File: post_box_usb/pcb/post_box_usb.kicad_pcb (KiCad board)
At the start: 4 copper layers, 90 x 45 mm, 63 parts, among them U1 MCP1700T-3302E/MB, X1 MC146 32768Hz

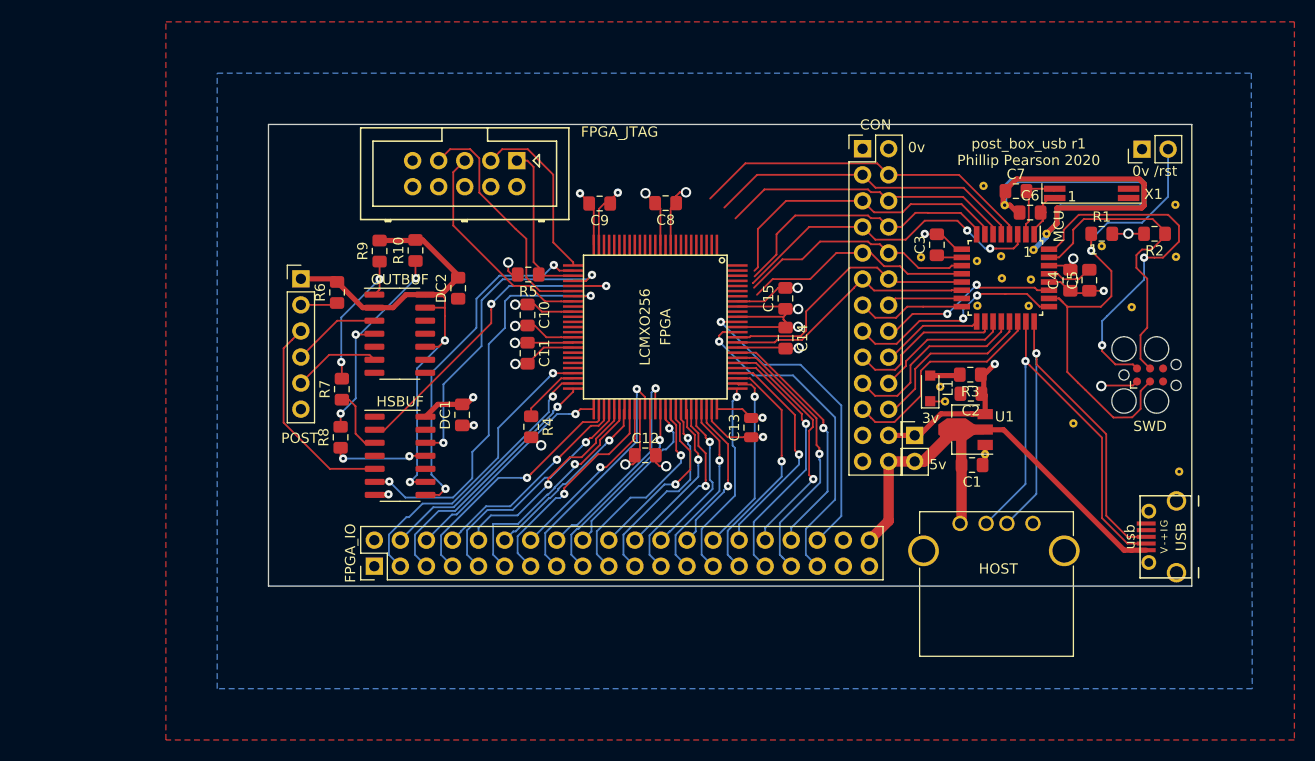
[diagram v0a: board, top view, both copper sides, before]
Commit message: Nearly done with the post_box_usb layout aside from a few TODOs in post_box_usb.py
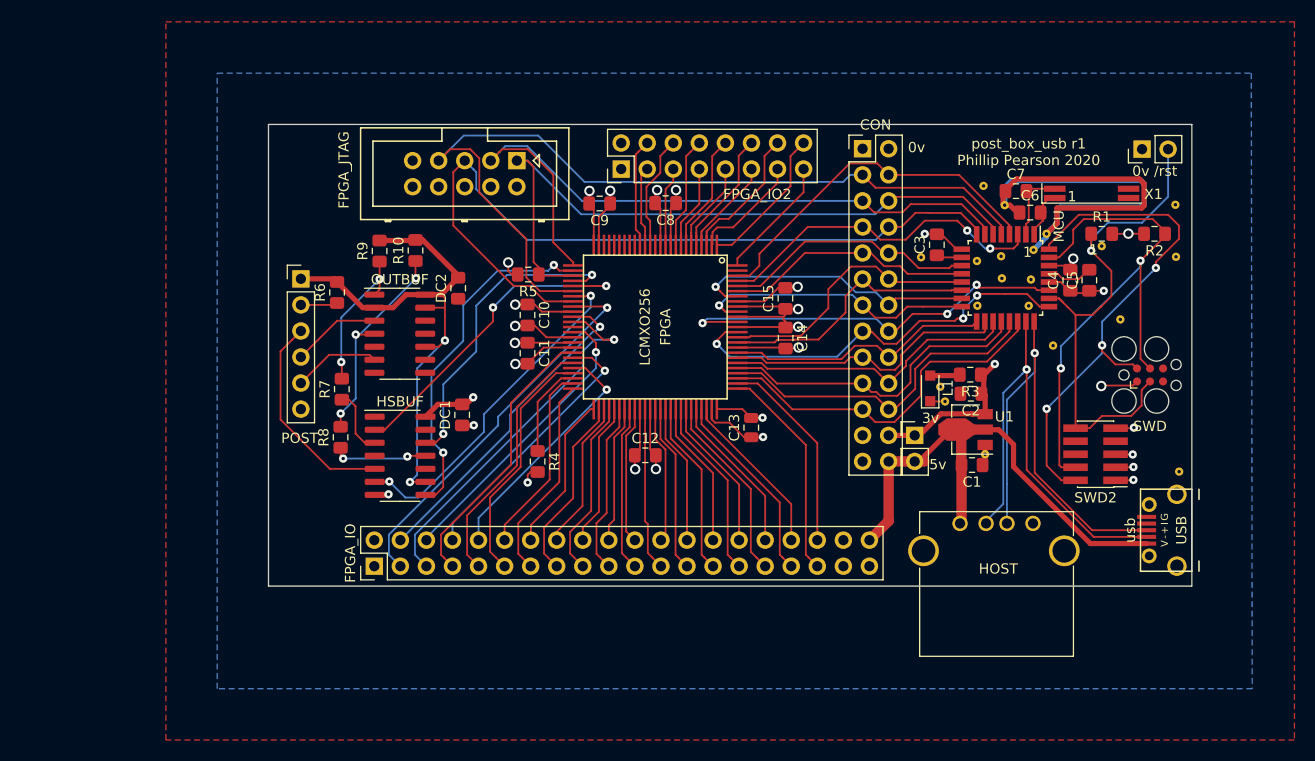
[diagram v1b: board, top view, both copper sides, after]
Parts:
- added FPGA_IO2: pins, Connector_PinHeader_2.54mm:PinHeader_2x08_P2.54mm_Vertical, F.Cu at (144.4, 134.3)
- added SWD2: swd, Connector_PinHeader_1.27mm:PinHeader_2x05_P1.27mm_Vertical_SMD, F.Cu at (190.6, 162.1)
- moved staple_single3 7.84 mm to (186.5, 151.6)
- moved R4 3.44 mm to (136.2, 162.9)
- moved staple_single11 1.63 mm to (193.0, 149.0)
- moved USB 0.65 mm to (198.0, 169.6)
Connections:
- CON pad 1: GND -> 3V3
- CON pad 3: PA04 -> fpga_TDO
- CON pad 5: PA06 -> fpga_TMS
- CON pad 6: PA05 -> fpga_TCK
- CON pad 8: PA07 -> fpga_TDI
- FPGA pad 1: (no net) -> fpga_GPIO47
- FPGA pad 100: (no net) -> fpga_GPIO46
- FPGA pad 11: (no net) -> fpga_GPIO36
- FPGA pad 14: (no net) -> fpga_GPIO37
- FPGA pad 15: (no net) -> fpga_GPIO34
- FPGA pad 16: (no net) -> fpga_GPIO35
- FPGA pad 2: (no net) -> fpga_GPIO44
- FPGA pad 3: (no net) -> fpga_GPIO45
- FPGA pad 34: (no net) -> fpga_GPIO0
- FPGA pad 36: (no net) -> fpga_GPIO1
- FPGA pad 37: (no net) -> fpga_GPIO2
- FPGA pad 38: (no net) -> fpga_OSC_in
- FPGA pad 39: (no net) -> fpga_GPIO3
- FPGA pad 4: (no net) -> fpga_GPIO42
- FPGA pad 43: (no net) -> fpga_GPIO4
- FPGA pad 44: (no net) -> fpga_GPIO5
- FPGA pad 45: (no net) -> fpga_GPIO6
- FPGA pad 46: (no net) -> fpga_GPIO7
- FPGA pad 47: fpga_GPIO0 -> fpga_GPIO8
- FPGA pad 49: fpga_GPIO1 -> fpga_GPIO9
- FPGA pad 5: (no net) -> fpga_GPIO43
- FPGA pad 50: fpga_GPIO2 -> fpga_GPIO10
- FPGA pad 51: fpga_GPIO3 -> fpga_GPIO11
- FPGA pad 52: fpga_GPIO4 -> fpga_GPIO12
- FPGA pad 53: fpga_GPIO5 -> fpga_GPIO13
- FPGA pad 54: fpga_GPIO6 -> fpga_GPIO14
- FPGA pad 55: fpga_GPIO7 -> fpga_GPIO15
- FPGA pad 56: fpga_GPIO8 -> fpga_GPIO16
- FPGA pad 57: fpga_GPIO9 -> fpga_GPIO17
- FPGA pad 58: fpga_GPIO10 -> fpga_GPIO18
- FPGA pad 59: fpga_GPIO11 -> fpga_GPIO19
- FPGA pad 6: (no net) -> fpga_GPIO40
- FPGA pad 61: fpga_GPIO12 -> fpga_GPIO20
- FPGA pad 63: fpga_GPIO13 -> fpga_GPIO21
- FPGA pad 64: fpga_GPIO14 -> fpga_GPIO22
- FPGA pad 65: fpga_GPIO15 -> fpga_GPIO23
- FPGA pad 66: fpga_GPIO16 -> fpga_GPIO24
- FPGA pad 67: fpga_GPIO17 -> fpga_GPIO25
- FPGA pad 68: fpga_GPIO18 -> fpga_GPIO26
- FPGA pad 69: fpga_GPIO19 -> fpga_GPIO27
- FPGA pad 7: (no net) -> fpga_GPIO41
- FPGA pad 70: fpga_GPIO20 -> fpga_GPIO28
- FPGA pad 71: fpga_GPIO21 -> fpga_GPIO29
- FPGA pad 72: fpga_GPIO22 -> fpga_GPIO30
- FPGA pad 73: fpga_GPIO23 -> fpga_GPIO31
- FPGA pad 76: fpga_GPIO24 -> fpga_GPIO32
- FPGA pad 77: fpga_GPIO25 -> fpga_GPIO33
- FPGA pad 78: fpga_GPIO26 -> mcu_RXD
- FPGA pad 79: fpga_GPIO27 -> mcu_TXD
- FPGA pad 8: (no net) -> fpga_GPIO38
- FPGA pad 80: fpga_GPIO28 -> PA19
- FPGA pad 81: fpga_GPIO29 -> PA18
- FPGA pad 82: fpga_GPIO30 -> want_tx
- FPGA pad 83: fpga_GPIO31 -> tx_pending
- FPGA pad 87: fpga_GPIO32 -> PA27
- FPGA pad 89: fpga_GPIO33 -> reset_in
- FPGA pad 9: (no net) -> fpga_GPIO39
- FPGA pad 91: (no net) -> fpga_MISO
- FPGA pad 94: (no net) -> fpga_SS
- FPGA pad 95: (no net) -> fpga_SCK
- FPGA pad 96: (no net) -> fpga_MOSI
- FPGA pad 97: (no net) -> last_transaction_was_input
- FPGA pad 98: (no net) -> PA03
- MCU pad 5: PA04 -> fpga_TDO
- MCU pad 6: PA05 -> fpga_TCK
- MCU pad 7: PA06 -> fpga_TMS
- MCU pad 8: PA07 -> fpga_TDI
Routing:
- net fpga_TDO: track 23.5 -> 84.4 mm
- net fpga_TDI: track 21.5 -> 77.9 mm
- net fpga_TMS: track 17.2 -> 70.6 mm
- net fpga_TCK: track 16.0 -> 67.2 mm
- net PA04: track 31.2 -> 0.00 mm
- net PA06: track 29.9 -> 0.00 mm
- net PA05: track 28.9 -> 0.00 mm
- net PA07: track 27.5 -> 0.00 mm
- net mcu_SWCLK: track 31.3 -> 54.8 mm, vias 0 -> 2
- net reset_in: track 17.7 -> 40.0 mm, vias 2 -> 3
- net fpga_SS: track 7.81 -> 28.7 mm, vias 0 -> 1
- net PA27: track 21.7 -> 40.1 mm, vias 2 -> 3
- net fpga_MISO: track 10.6 -> 27.5 mm, vias 0 -> 1
- net mcu_TXD: track 17.0 -> 33.2 mm
- net tx_pending: track 10.4 -> 26.4 mm
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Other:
- board text added: "post_box_usb r1 Copyright 2017-2020 Google Inc Designed by Phillip Pearson github.com/google/myelin-acorn-electron-hardware myelin.nz/acorn/postbox"
- board text removed: "post_box_usb Copyright 2017-2020 Google Inc Designed by Phillip Pearson github.com/google/ myelin-acorn-electron-hardware"

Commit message: post_box_usb PCB r1 finished and sent to JLCPCB
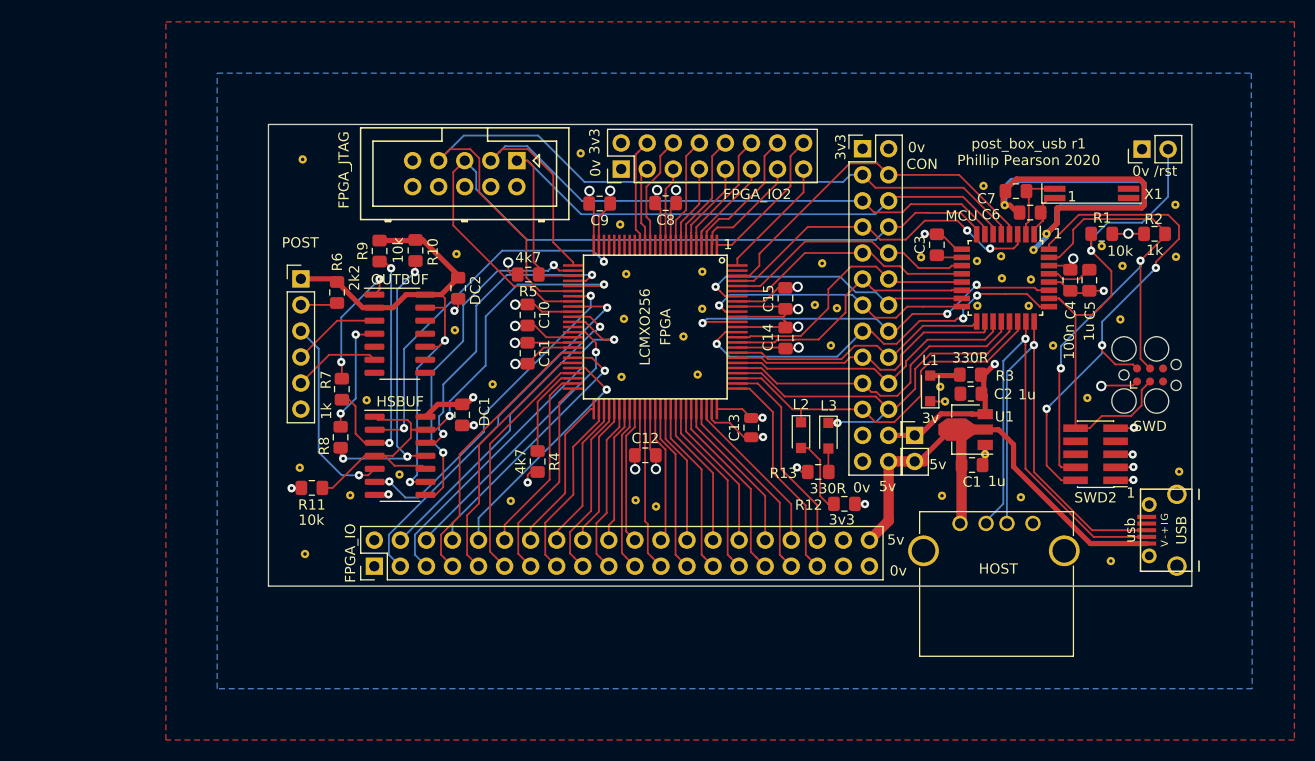
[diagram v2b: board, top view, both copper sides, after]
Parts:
- added L2: led, Diode_SMD:D_SOD-323_HandSoldering, F.Cu at (161.9, 160.3)
- added L3: led, Diode_SMD:D_SOD-323_HandSoldering, F.Cu at (164.6, 160.3)
- added R11: 10k, Resistor_SMD:R_0805_2012Metric_Pad1.15x1.40mm_HandSolder, F.Cu at (114.2, 165.4)
- added R12: 330R, Resistor_SMD:R_0805_2012Metric_Pad1.15x1.40mm_HandSolder, F.Cu at (166.1, 167.0)
- added R13: 330R, Resistor_SMD:R_0805_2012Metric_Pad1.15x1.40mm_HandSolder, F.Cu at (163.6, 163.9)
- added staple_single21: , myelin-kicad:via_single, F.Cu at (113.6, 171.9)
- added staple_single22: , myelin-kicad:via_single, F.Cu at (140.4, 132.8)
- added staple_single23: , myelin-kicad:via_single, F.Cu at (113.3, 133.4)
- added staple_single24: , myelin-kicad:via_single, F.Cu at (119.6, 156.9)
- added staple_single25: , myelin-kicad:via_single, F.Cu at (113.0, 163.5)
- added staple_single26: , myelin-kicad:via_single, F.Cu at (144.9, 144.6)
- added staple_single27: , myelin-kicad:via_single, F.Cu at (164.8, 151.6)
- added staple_single28: , myelin-kicad:via_single, F.Cu at (118.0, 166.2)
- added staple_single29: , myelin-kicad:via_single, F.Cu at (151.8, 154.4)
- added staple_single30: , myelin-kicad:via_single, F.Cu at (152.3, 144.3)
- added staple_single31: , myelin-kicad:via_single, F.Cu at (122.8, 164.1)
- added staple_single32: , myelin-kicad:via_single, F.Cu at (128.2, 150.1)
- added staple_single33: , myelin-kicad:via_single, F.Cu at (128.3, 142.6)
- added staple_single34: , myelin-kicad:via_single, F.Cu at (144.4, 154.6)
- added staple_single35: , myelin-kicad:via_single, F.Cu at (175.7, 166.2)
- added staple_single36: , myelin-kicad:via_single, F.Cu at (144.3, 139.8)
- added staple_single37: , myelin-kicad:via_single, F.Cu at (144.7, 148.9)
- added staple_single38: , myelin-kicad:via_single, F.Cu at (133.6, 166.7)
- added staple_single39: , myelin-kicad:via_single, F.Cu at (183.3, 166.3)
- added staple_single40: , myelin-kicad:via_single, F.Cu at (131.8, 155.3)
- added staple_single41: , myelin-kicad:via_single, F.Cu at (152.3, 148.0)
- added staple_single42: , myelin-kicad:via_single, F.Cu at (145.8, 166.6)
- added staple_single43: , myelin-kicad:via_single, F.Cu at (192.1, 172.6)
- added staple_single44: , myelin-kicad:via_single, F.Cu at (193.2, 143.8)
- added staple_single45: , myelin-kicad:via_single, F.Cu at (164.0, 143.5)
- added staple_single46: , myelin-kicad:via_single, F.Cu at (147.8, 167.2)
- added staple_single47: , myelin-kicad:via_single, F.Cu at (150.4, 150.7)
- added staple_single48: , myelin-kicad:via_single, F.Cu at (189.8, 156.7)
- added staple_single49: , myelin-kicad:via_single, F.Cu at (163.3, 147.6)
- added staple_single50: , myelin-kicad:via_single, F.Cu at (165.4, 147.9)
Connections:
- net fpga_MISO renamed fpga_spi_miso
- net fpga_MOSI renamed fpga_spi_mosi
- net fpga_SCK renamed fpga_spi_sck
- net fpga_SS renamed fpga_spi_cs
- net want_tx renamed target_power_out
- FPGA pad 23: (no net) -> testack_noe
- FPGA pad 30: testack_noe -> hotswap_noe
- HSBUF pad 1: GND -> hotswap_noe
- HSBUF pad 10: GND -> hotswap_noe
- HSBUF pad 13: GND -> hotswap_noe
- HSBUF pad 4: GND -> hotswap_noe
- R10 pad 1: target_reset_noe_buf_r -> target_reset_noe_buf
- R9 pad 1: testack_noe_buf_r -> testack_noe_buf
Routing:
- net hotswap_noe: track 0.00 -> 52.7 mm, vias 0 -> 2
- net target_reset_noe_buf: track 9.29 -> 29.5 mm, vias 2 -> 3
- net testack_noe_buf: track 6.51 -> 26.4 mm, vias 0 -> 2
- net target_reset_noe_buf_r: track 21.3 -> 11.5 mm, vias 3 -> 2
- net mcu_txd_led_anode: track 0.00 -> 7.51 mm
- net mcu_TXD: track 33.2 -> 39.7 mm, vias 0 -> 1
- net testack_noe: track 32.4 -> 36.2 mm
- net 3V3: track 94.1 -> 97.2 mm, vias 16 -> 19
- net USBDM: track 45.6 -> 48.6 mm
- net mcu_rxd_led_anode: track 0.00 -> 2.30 mm
- net testack_noe_buf_r: track 14.7 -> 13.0 mm
- net testreq: track 20.6 -> 19.2 mm, vias 0 -> 1
- net GND: track 130.9 -> 132.3 mm, vias 15 -> 16
- net mcu_RXD: track 35.1 -> 36.4 mm
- net USBDP: track 45.7 -> 46.5 mm
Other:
- board text added: "3v3"

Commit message: post_box_usb: Changed MCU connections to suit the synchronous FPGA design rather than the old slave SPI code
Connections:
- net last_transaction_was_input renamed PA02
- net tx_pending renamed PA16
- CON pad 11: rx_ready -> target_power_out
- CON pad 17: target_power_out -> PA17
- FPGA pad 82: target_power_out -> PA17
- FPGA pad 85: rx_ready -> target_power_out
- MCU pad 14: rx_ready -> target_power_out
- MCU pad 18: target_power_out -> PA17
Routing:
- net PA17: track 0.00 -> 28.1 mm
- net rx_ready: track 25.8 -> 0.00 mm
- net target_power_out: track 28.1 -> 25.8 mm

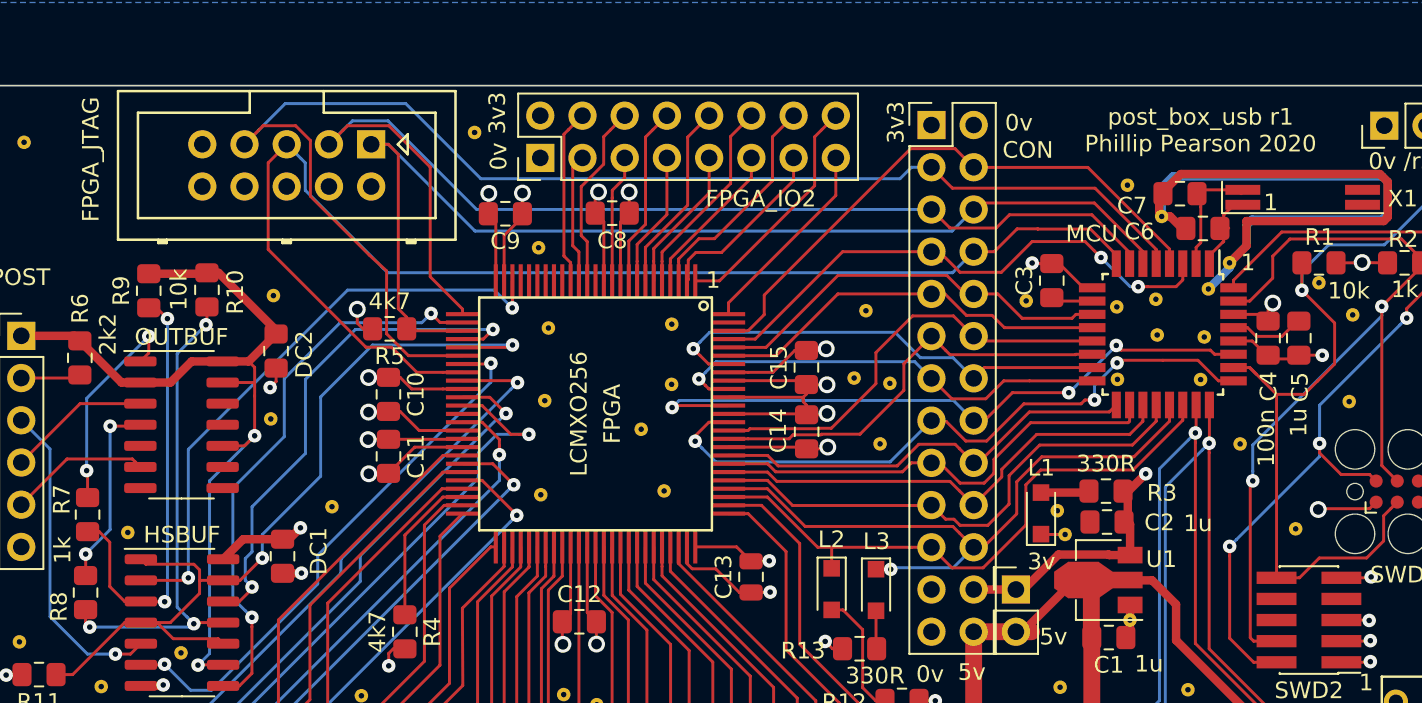
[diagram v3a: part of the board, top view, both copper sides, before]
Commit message: post_box_usb: Added BOM and silkscreen updates for r2
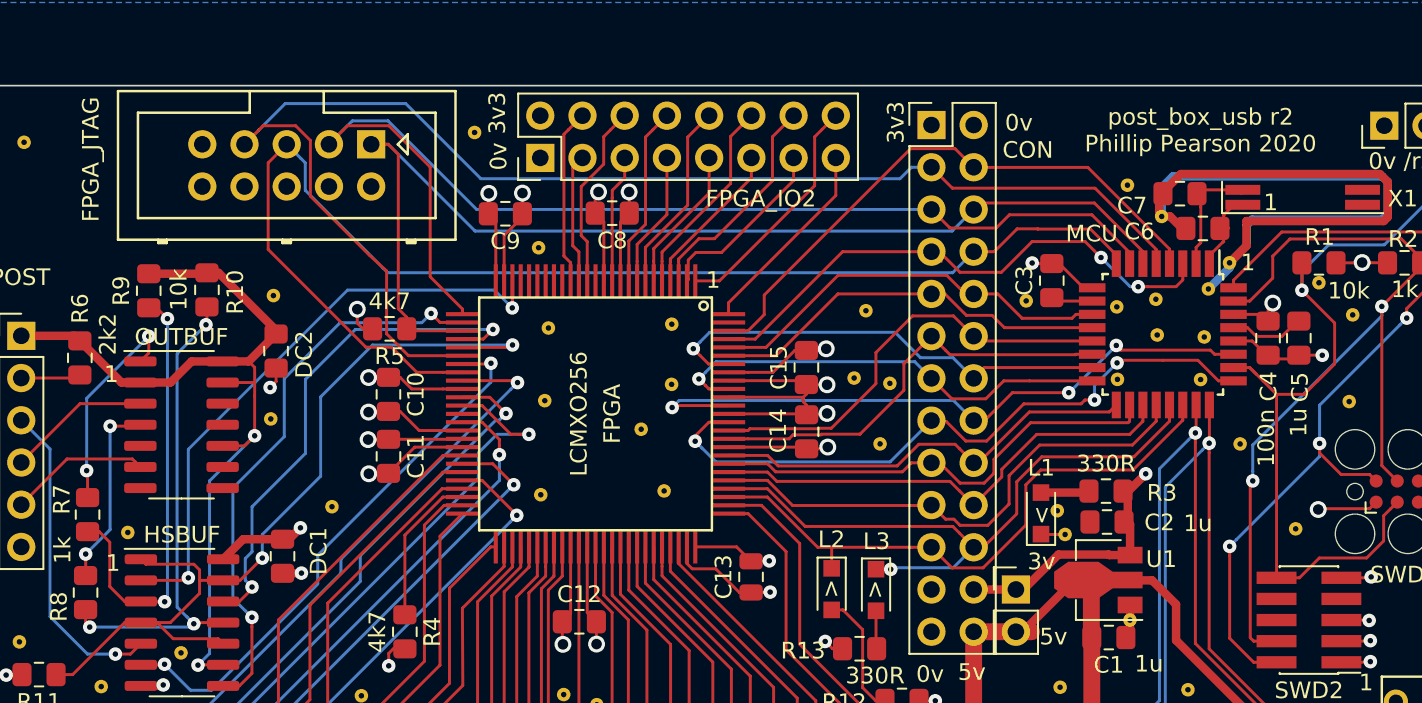
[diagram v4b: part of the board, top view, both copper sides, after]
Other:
- board text added: ">"
- board text added: "post_box_usb r2 Phillip Pearson 2020"
- board text removed: "post_box_usb r1 Phillip Pearson 2020"
